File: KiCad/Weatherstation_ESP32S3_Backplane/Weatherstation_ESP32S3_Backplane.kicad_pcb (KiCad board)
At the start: 2 copper layers, 99.9 x 99.9 mm, 68 parts, among them J1 01x02 JST XH, J10 01x04 Molex KK254, J11 01x02 JST XH, J12 01x04 Molex KK254, J13 01x22 Generic socket, J14 01x22 Generic socket, J15 01x02 JST XH, J16 01x04 Molex KK254, J17 01x02 JST XH, J18 01x06 Generic socket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

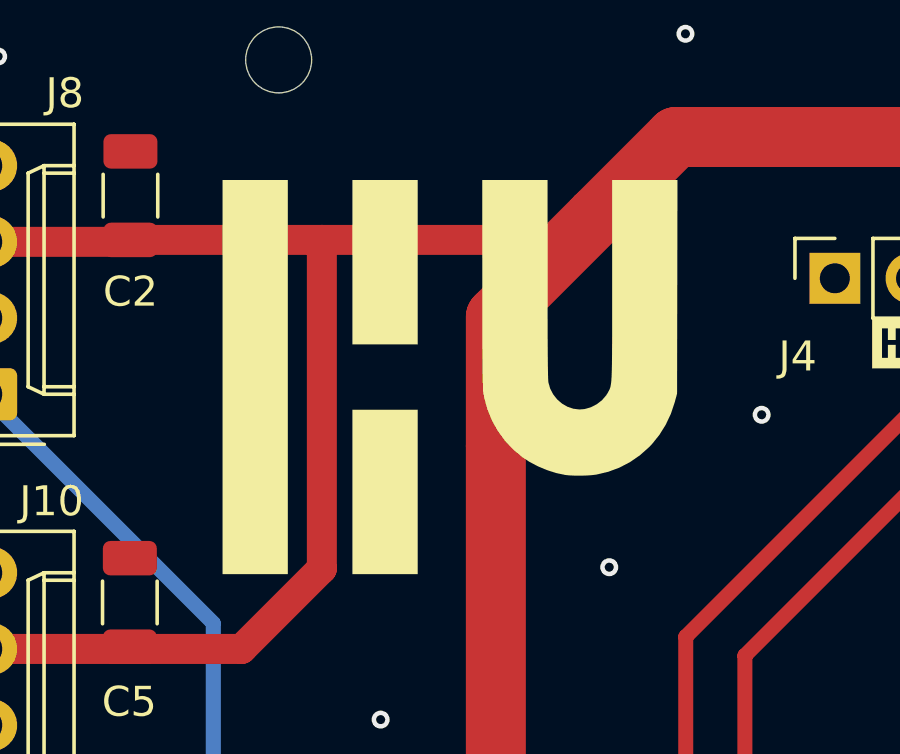
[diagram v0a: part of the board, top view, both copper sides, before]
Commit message: Changed the HU-logo from silkscreen to soldermask punch-out
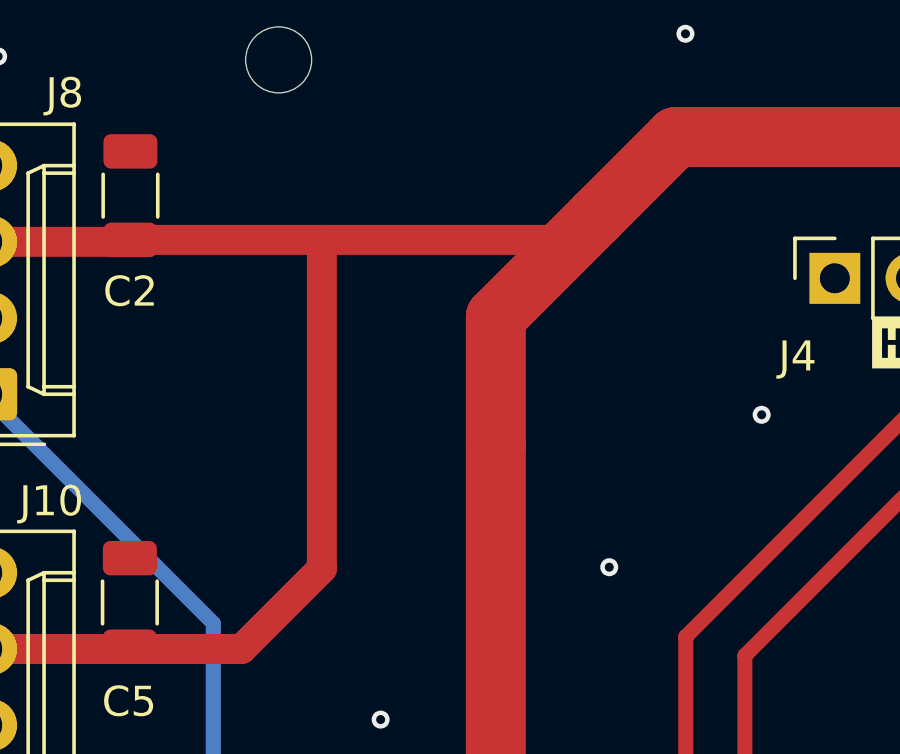
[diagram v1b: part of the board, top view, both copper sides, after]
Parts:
- removed the G*** at (154.7, 52.1)
- added G***: LOGO, LOGO, F.Cu at (220.9, 38.9)
- added G***: LOGO, LOGO, B.Cu at (220.9, 39.0)

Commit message: Moved HU-logo
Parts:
- moved G*** 1.02 mm to (219.8, 39.0) (x2)
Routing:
- net GND: vias 187 -> 186
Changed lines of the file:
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@@
   )
   (footprint "LOGO" (layer "F.Cu")
-    (at 220.857204 38.943747)
+    (at 219.837204 39.013747)
     (attr board_only exclude_from_pos_files exclude_from_bom)
     (fp_text reference "G***" (at 0 0) (layer "F.SilkS") hide
@@
   )
   (footprint "LOGO" (layer "B.Cu")
-    (at 220.87 38.95 180)
+    (at 219.85 39.02 180)
     (attr board_only exclude_from_pos_files exclude_from_bom)
     (fp_text reference "G***" (at 0 0) (layer "B.SilkS") hide
@@
   (via (at 133.12 105.081819) (size 0.6) (drill 0.3) (layers "F.Cu" "B.Cu") (free) (net 2))
   (via (at 219.856361 132) (size 0.6) (drill 0.3) (layers "F.Cu" "B.Cu") (free) (net 2))
-  (via (at 215.9 40.64) (size 0.6) (drill 0.3) (layers "F.Cu" "B.Cu") (free) (net 2))
   (via (at 133.12 81.154547) (size 0.6) (drill 0.3) (layers "F.Cu" "B.Cu") (free) (net 2))
   (via (at 199.36 122.95) (size 0.6) (drill 0.3) (layers "F.Cu" "B.Cu") (free) (net 2))
